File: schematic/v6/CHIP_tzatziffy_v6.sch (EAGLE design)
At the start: 57 parts, among them J1 2X20-CHIP0.8_DRILL, Q2 2N7002ET1G, Q3 BSS7728NH6327XTSA2, U1 LMR62421, U3 DS2431P, X1 FH12-40S-0.5SH

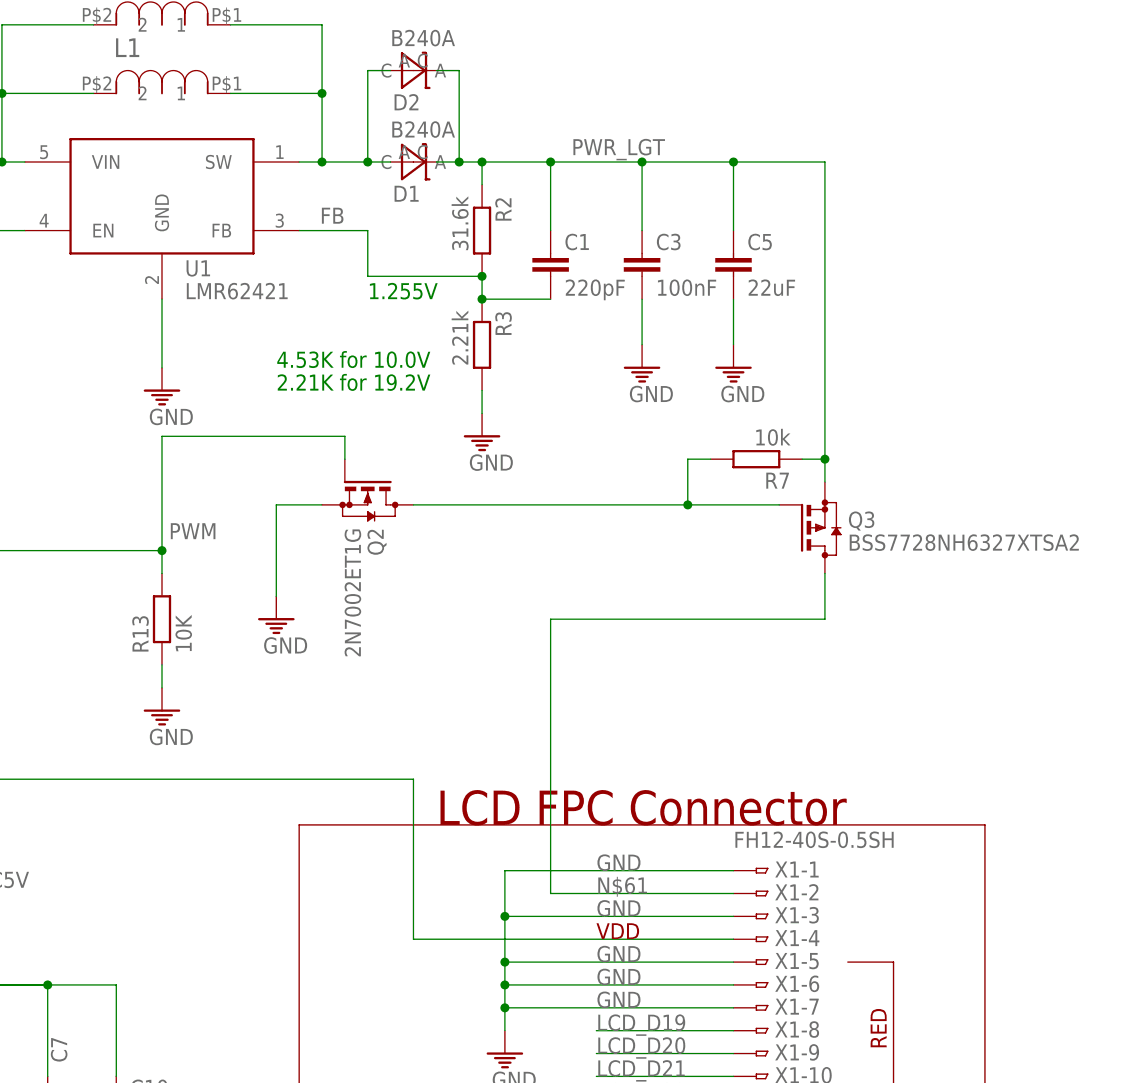
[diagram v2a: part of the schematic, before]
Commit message: simplyfied the backlight driver ... a lot
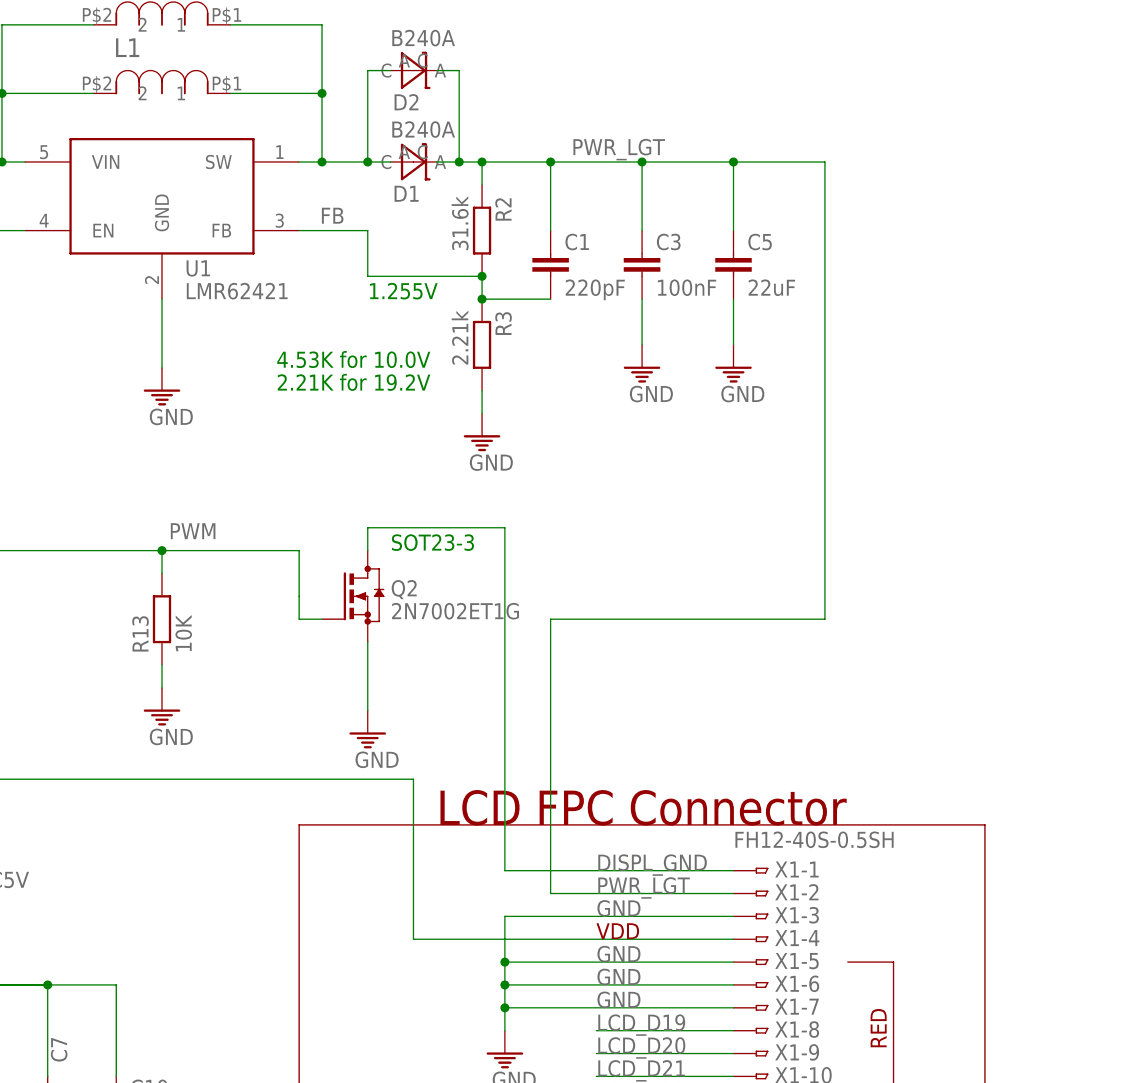
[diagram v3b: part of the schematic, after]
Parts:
- removed Q3: BSS7728NH6327XTSA2, transistor-small-signal:BSS84
- removed R7: 10k, rcl:R-EU_M0805
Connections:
- removed net N$61: Q3.D, X1-2.1
- removed net N$9: Q2.D, Q3.G, R7.2
- new net DISPL_GND: Q2.D, X1-1.1
- net GND: no longer X1-1.1
- net PWR_LGT: now also X1-2.1; no longer Q3.S, R7.1
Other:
- note added: "SOT23-3"
- moved on the sheet: Q2
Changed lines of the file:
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@@
 <part name="VBAT" library="wirepad" deviceset="1,6/0,8" device=""/>
 <part name="CHRIN" library="wirepad" deviceset="1,6/0,8" device=""/>
-<part name="Q3" library="transistor-small-signal" deviceset="BSS84" device="" value="BSS7728NH6327XTSA2"/>
-<part name="R7" library="rcl" deviceset="R-EU_" device="M0805" value="10k"/>
 <part name="U$7" library="Keyboard v0.2" deviceset="GND" device=""/>
 <part name="Q2" library="transistor-small-signal" deviceset="BSS123" device="" value="2N7002ET1G"/>
@@
 <text x="520.7" y="236.22" size="1.778" layer="91">2.21K for 19.2V</text>
 <text x="368.3" y="210.82" size="1.778" layer="99">cut here -&gt;</text>
+<text x="533.4" y="218.44" size="1.778" layer="91">SOT23-3</text>
 </plain>
 <instances>
@@
 <instance part="VBAT" gate="P" x="281.94" y="198.12"/>
 <instance part="CHRIN" gate="P" x="236.22" y="142.24" rot="R270"/>
-<instance part="Q3" gate="G$1" x="581.66" y="220.98"/>
-<instance part="R7" gate="G$1" x="574.04" y="228.6" rot="R180"/>
-<instance part="U$7" gate="M" x="520.7" y="210.82"/>
-<instance part="Q2" gate="G$1" x="530.86" y="223.52" rot="R270"/>
+<instance part="U$7" gate="M" x="530.86" y="198.12"/>
+<instance part="Q2" gate="G$1" x="530.86" y="213.36"/>
 </instances>
 <busses>
@@
 <segment>
 <pinref part="U$17" gate="M" pin="GND"/>
-<wire x1="546.1" y1="182.88" x2="546.1" y2="177.8" width="0.1524" layer="91"/>
 <label x="556.26" y="172.72" size="1.778" layer="95"/>
 <label x="556.26" y="170.18" size="1.778" layer="95"/>
 <label x="556.26" y="177.8" size="1.778" layer="95"/>
-<label x="556.26" y="182.88" size="1.778" layer="95"/>
 <wire x1="546.1" y1="177.8" x2="546.1" y2="172.72" width="0.1524" layer="91"/>
 <wire x1="546.1" y1="172.72" x2="546.1" y2="170.18" width="0.1524" layer="91"/>
@@
 <pinref part="X1" gate="-3" pin="1"/>
 <wire x1="571.5" y1="177.8" x2="546.1" y2="177.8" width="0.1524" layer="91"/>
-<junction x="546.1" y="177.8"/>
-<pinref part="X1" gate="-1" pin="1"/>
-<wire x1="571.5" y1="182.88" x2="546.1" y2="182.88" width="0.1524" layer="91"/>
 <pinref part="X1" gate="-7" pin="1"/>
 <wire x1="571.5" y1="167.64" x2="546.1" y2="167.64" width="0.1524" layer="91"/>
@@
 </segment>
 <segment>
-<wire x1="525.78" y1="223.52" x2="520.7" y2="223.52" width="0.1524" layer="91"/>
-<wire x1="520.7" y1="223.52" x2="520.7" y2="213.36" width="0.1524" layer="91"/>
+<wire x1="530.86" y1="208.28" x2="530.86" y2="200.66" width="0.1524" layer="91"/>
 <pinref part="U$7" gate="M" pin="GND"/>
 <pinref part="Q2" gate="G$1" pin="S"/>
@@
 <label x="563.88" y="264.16" size="1.778" layer="95" rot="R180"/>
 <wire x1="571.5" y1="261.62" x2="581.66" y2="261.62" width="0.1524" layer="91"/>
-<wire x1="581.66" y1="261.62" x2="581.66" y2="228.6" width="0.1524" layer="91"/>
+<wire x1="581.66" y1="261.62" x2="581.66" y2="210.82" width="0.1524" layer="91"/>
 <junction x="571.5" y="261.62"/>
 <pinref part="D1" gate="G$1" pin="C"/>
-<wire x1="581.66" y1="228.6" x2="581.66" y2="226.06" width="0.1524" layer="91"/>
 <wire x1="538.48" y1="261.62" x2="541.02" y2="261.62" width="0.1524" layer="91"/>
 <wire x1="541.02" y1="261.62" x2="543.56" y2="261.62" width="0.1524" layer="91"/>
@@
 <wire x1="541.02" y1="271.78" x2="541.02" y2="261.62" width="0.1524" layer="91"/>
 <junction x="541.02" y="261.62"/>
-<pinref part="Q3" gate="G$1" pin="S"/>
-<pinref part="R7" gate="G$1" pin="1"/>
-<wire x1="579.12" y1="228.6" x2="581.66" y2="228.6" width="0.1524" layer="91"/>
-<junction x="581.66" y="228.6"/>
+<pinref part="X1" gate="-2" pin="1"/>
+<wire x1="571.5" y1="180.34" x2="551.18" y2="180.34" width="0.1524" layer="91"/>
+<wire x1="551.18" y1="180.34" x2="551.18" y2="210.82" width="0.1524" layer="91"/>
+<label x="556.26" y="180.34" size="1.778" layer="95"/>
+<wire x1="551.18" y1="210.82" x2="581.66" y2="210.82" width="0.1524" layer="91"/>
 </segment>
 </net>
@@
 </segment>
 </net>
-<net name="N$61" class="0">
-<segment>
-<pinref part="X1" gate="-2" pin="1"/>
-<wire x1="571.5" y1="180.34" x2="551.18" y2="180.34" width="0.1524" layer="91"/>
-<wire x1="551.18" y1="180.34" x2="551.18" y2="210.82" width="0.1524" layer="91"/>
-<label x="556.26" y="180.34" size="1.778" layer="95"/>
-<pinref part="Q3" gate="G$1" pin="D"/>
-<wire x1="551.18" y1="210.82" x2="581.66" y2="210.82" width="0.1524" layer="91"/>
-<wire x1="581.66" y1="210.82" x2="581.66" y2="215.9" width="0.1524" layer="91"/>
-</segment>
-</net>
 <net name="PWM" class="0">
 <segment>
@@
 <wire x1="424.18" y1="218.44" x2="508" y2="218.44" width="0.1524" layer="91"/>
 <pinref part="Q2" gate="G$1" pin="G"/>
-<wire x1="528.32" y1="228.6" x2="528.32" y2="231.14" width="0.1524" layer="91"/>
-<wire x1="528.32" y1="231.14" x2="508" y2="231.14" width="0.1524" layer="91"/>
-<wire x1="508" y1="231.14" x2="508" y2="218.44" width="0.1524" layer="91"/>
+<wire x1="525.78" y1="210.82" x2="523.24" y2="210.82" width="0.1524" layer="91"/>
+<wire x1="523.24" y1="210.82" x2="523.24" y2="213.36" width="0.1524" layer="91"/>
+<wire x1="523.24" y1="213.36" x2="523.24" y2="218.44" width="0.1524" layer="91"/>
+<wire x1="523.24" y1="218.44" x2="508" y2="218.44" width="0.1524" layer="91"/>
 <junction x="508" y="218.44"/>
 </segment>
@@
 </segment>
 </net>
-<net name="N$9" class="0">
-<segment>
-<pinref part="Q3" gate="G$1" pin="G"/>
-<pinref part="R7" gate="G$1" pin="2"/>
-<wire x1="576.58" y1="223.52" x2="566.42" y2="223.52" width="0.1524" layer="91"/>
-<wire x1="566.42" y1="223.52" x2="535.94" y2="223.52" width="0.1524" layer="91"/>
-<wire x1="568.96" y1="228.6" x2="566.42" y2="228.6" width="0.1524" layer="91"/>
-<wire x1="566.42" y1="228.6" x2="566.42" y2="223.52" width="0.1524" layer="91"/>
-<junction x="566.42" y="223.52"/>
+<net name="DISPL_GND" class="0">
+<segment>
+<pinref part="X1" gate="-1" pin="1"/>
+<wire x1="571.5" y1="182.88" x2="546.1" y2="182.88" width="0.1524" layer="91"/>
+<label x="556.26" y="182.88" size="1.778" layer="95"/>
+<wire x1="546.1" y1="182.88" x2="546.1" y2="220.98" width="0.1524" layer="91"/>
 <pinref part="Q2" gate="G$1" pin="D"/>
-</segment>
-</net>
+<wire x1="546.1" y1="220.98" x2="530.86" y2="220.98" width="0.1524" layer="91"/>
+<wire x1="530.86" y1="220.98" x2="530.86" y2="218.44" width="0.1524" layer="91"/>
+</segment>
+</net>

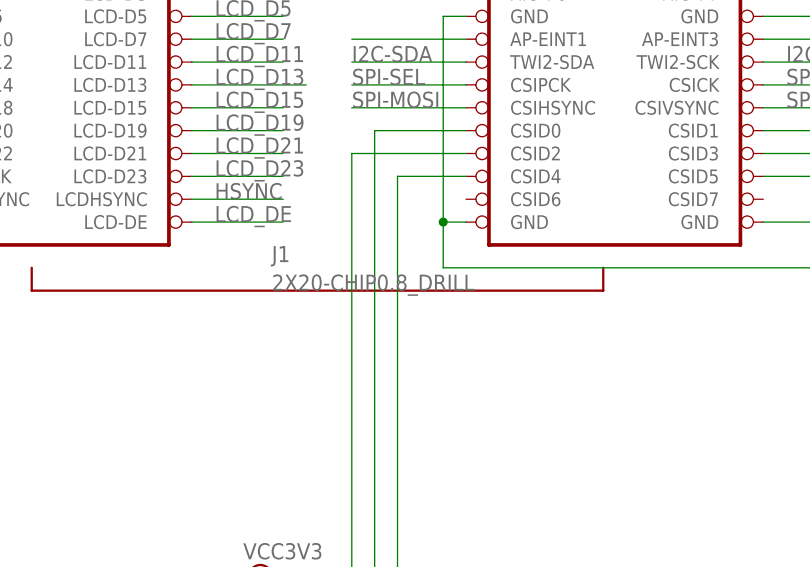
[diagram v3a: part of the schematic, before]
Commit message: changed holes size to 0.7mm
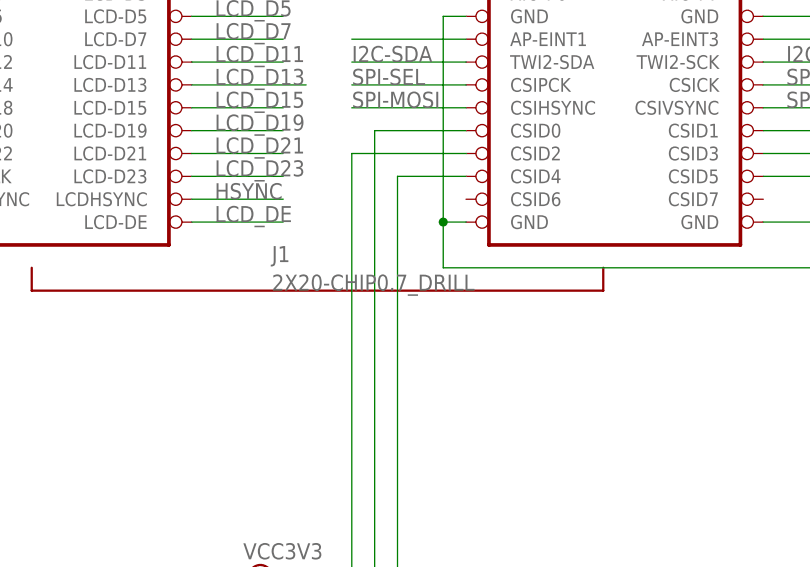
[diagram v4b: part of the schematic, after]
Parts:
- J1: value 2X20-CHIP0.8_DRILL -> 2X20-CHIP0.7_DRILL; device JKW_CHIP:2X20-CHIP0.8_DRILL -> JKW_CHIP:2X20-CHIP0.7_DRILL
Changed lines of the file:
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@@
 <part name="R13" library="rcl" deviceset="R-EU_" device="M0805" value="10K"/>
 <part name="U$40" library="Keyboard v0.2" deviceset="GND" device=""/>
-<part name="J1" library="JKW_CHIP" deviceset="2X20-CHIP" device="0.8_DRILL" value="2X20-CHIP0.8_DRILL"/>
+<part name="J1" library="JKW_CHIP" deviceset="2X20-CHIP" device="0.7_DRILL" value="2X20-CHIP0.7_DRILL"/>
 <part name="GND2" library="supply1" deviceset="GND" device=""/>
 <part name="SDIO" library="JKW_CHIP" deviceset="TF-HOLDER" device=""/>
